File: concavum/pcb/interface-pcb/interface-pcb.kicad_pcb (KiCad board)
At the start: 2 copper layers, 29 x 38 mm, 20 parts, among them J1 USB_C_Port, J2 Audio_Jack, J3 ISP_pads, J4 FPC_connector, U1 ATmega32U4-A, U2 MCP23017_SO, Y1 Crystal_16MHz

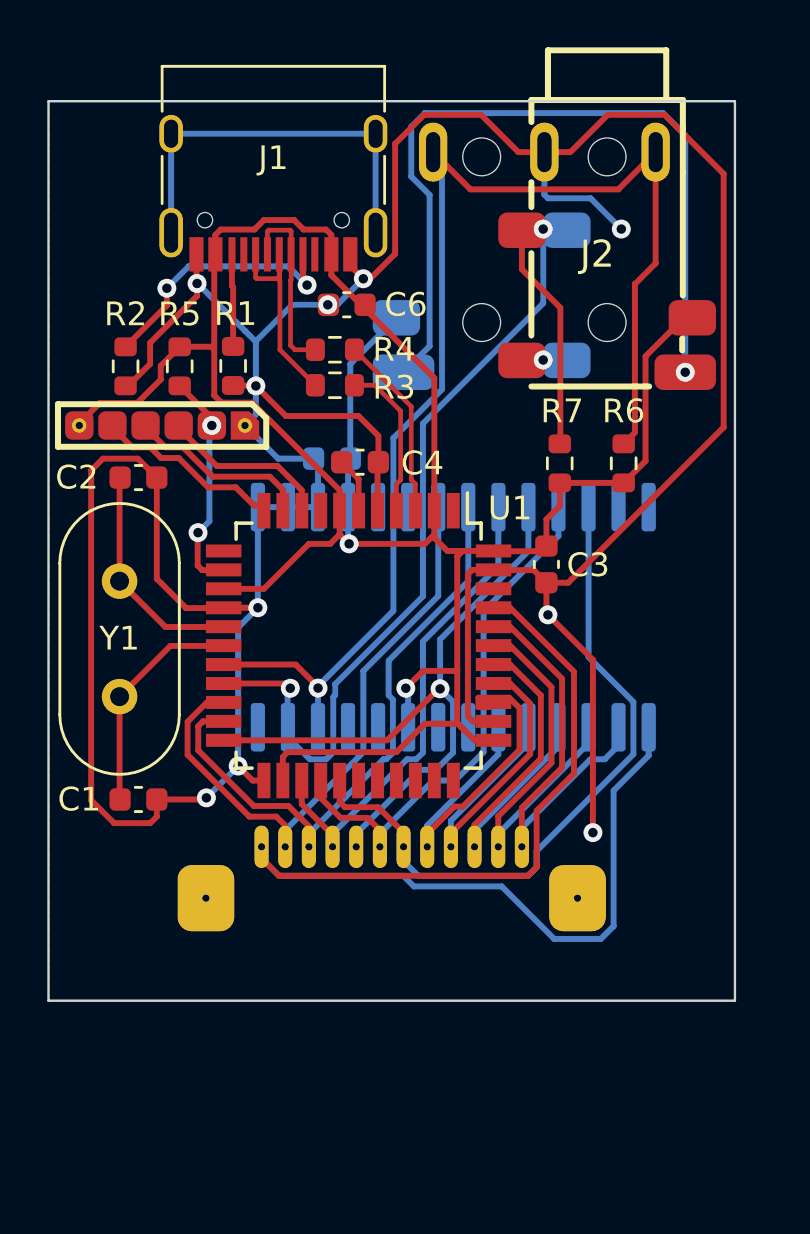
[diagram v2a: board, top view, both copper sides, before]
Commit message: Improve footprints
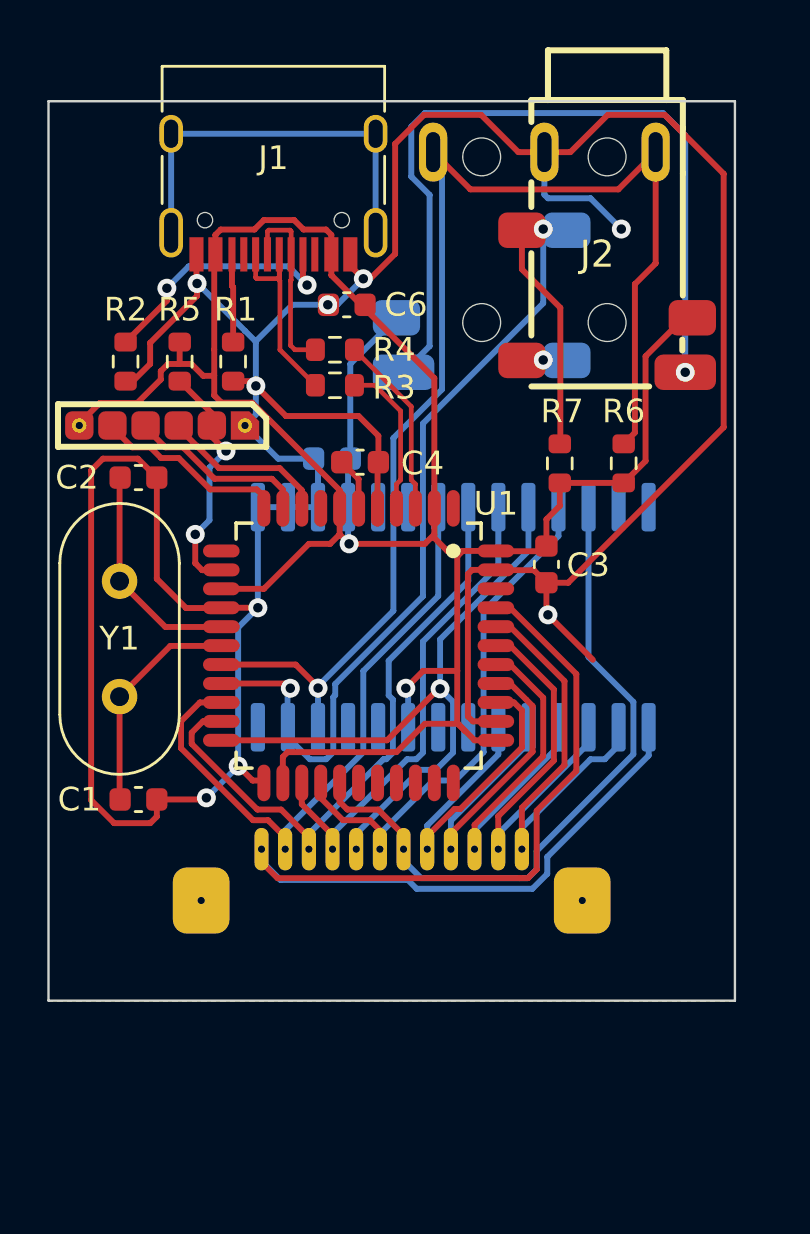
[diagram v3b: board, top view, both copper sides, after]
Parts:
- U1: footprint Package_QFP:TQFP-44_10x10mm_P0.8mm -> Custom:TQFP-44-Rounded-Pads
- moved R2 0.20 mm to (143.3, 91.0)
- moved R5 0.20 mm to (145.5, 91.0)
- moved R1 0.19 mm to (147.8, 91.0)
- moved J4 0.10 mm to (154.5, 111.6)
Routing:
- net GND: track 157.6 -> 150.3 mm, vias 10 -> 9
- net /ROW1: track 52.0 -> 47.5 mm
- net /ROW2: track 17.0 -> 16.0 mm
- net /RST: track 9.35 -> 10.1 mm
- net /COL6: track 28.8 -> 29.6 mm
- net +5V: track 104.9 -> 105.6 mm
